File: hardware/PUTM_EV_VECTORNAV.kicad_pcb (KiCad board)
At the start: 2 copper layers, 60 x 40 mm, 4 parts

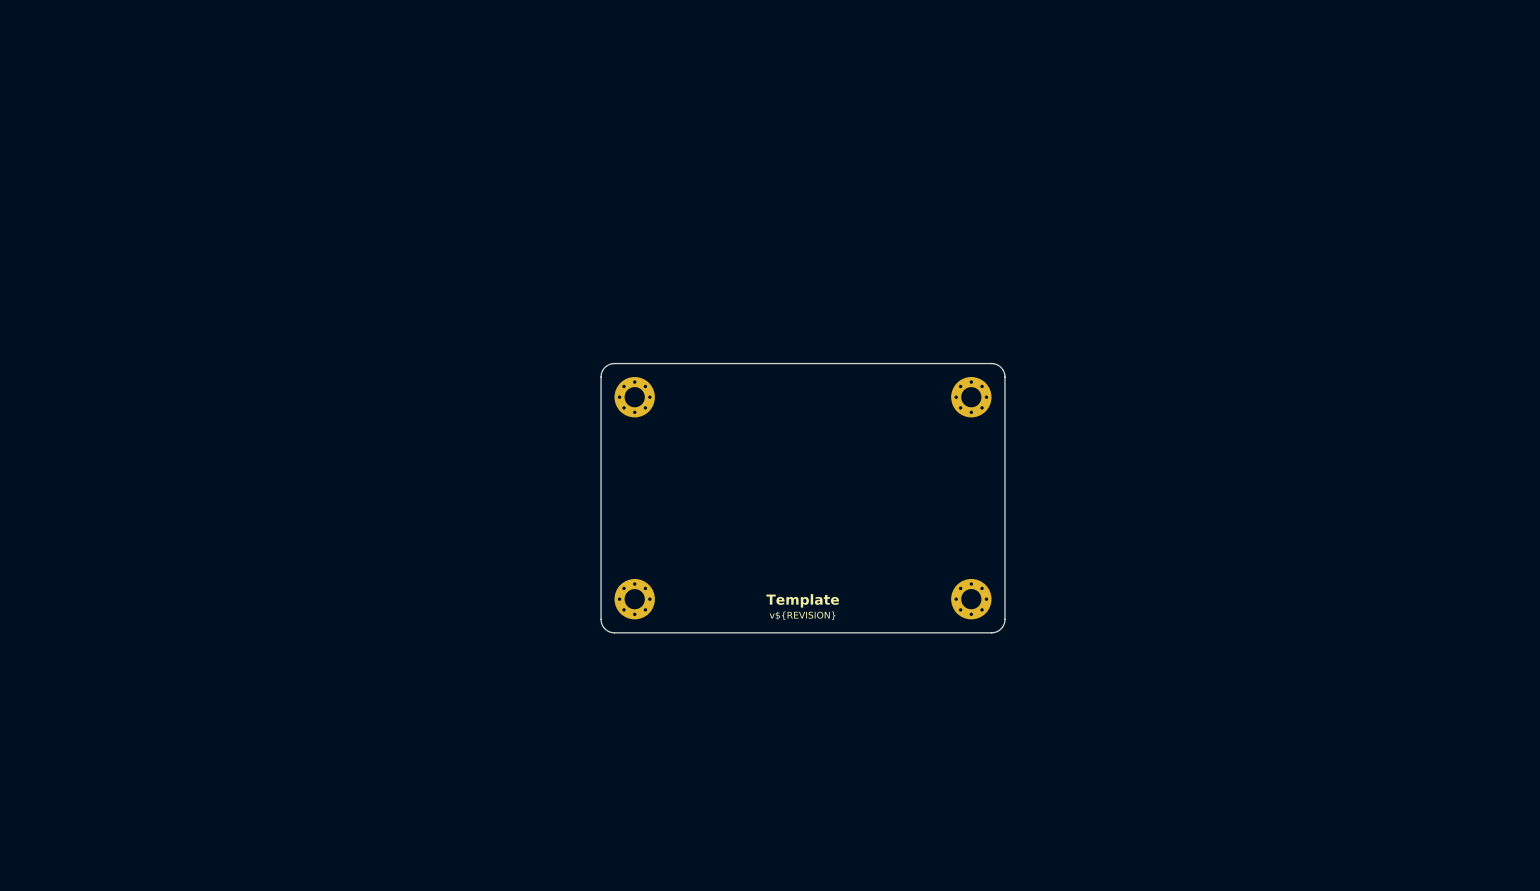
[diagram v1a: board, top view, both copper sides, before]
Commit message: 3D models, optocoupler added, pcb settings and components placing
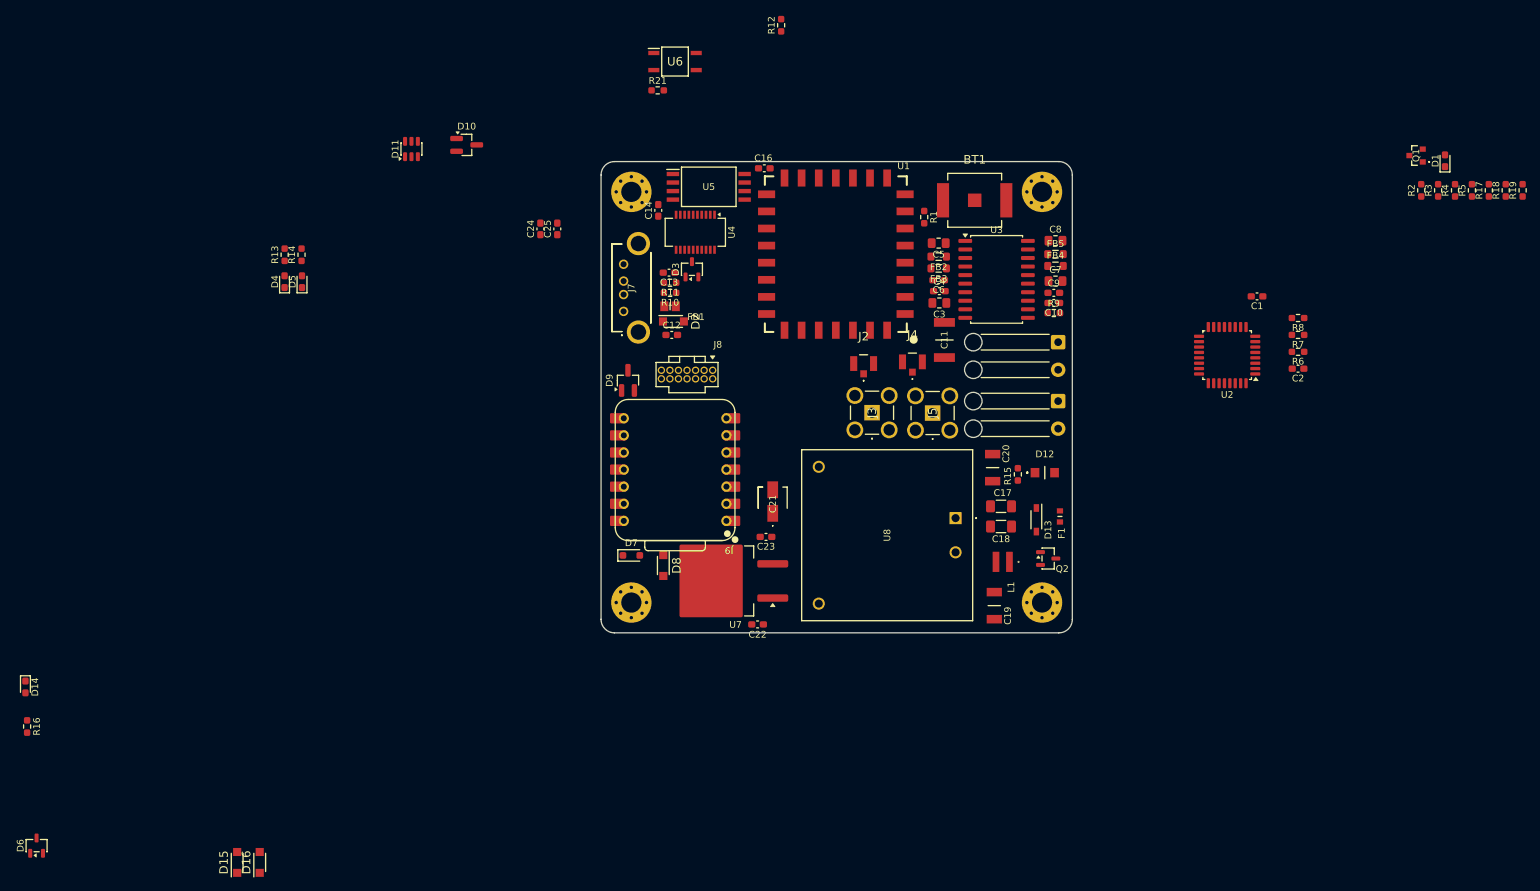
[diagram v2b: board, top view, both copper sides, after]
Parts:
- added BT1: Battery_Cell, BatteryHolder:2998TR, F.Cu at (171.5, 51.8)
- added C1: 100nF, Capacitor_SMD:C_0603_1608Metric_Pad1.08x0.95mm_HandSolder, F.Cu at (213.4, 66.0)
- added C10: 10nF, Capacitor_SMD:C_0603_1608Metric_Pad1.08x0.95mm_HandSolder, F.Cu at (183.2, 67.0)
- added C11: 4.7nF/Y2, samacsys:CAPC5728X280N, F.Cu at (167.0, 72.5)
- added C12: 10nF, Capacitor_SMD:C_0603_1608Metric_Pad1.08x0.95mm_HandSolder, F.Cu at (126.5, 71.8)
- added C13: 100nF, Capacitor_SMD:C_0603_1608Metric_Pad1.08x0.95mm_HandSolder, F.Cu at (126.1, 62.5)
- added C14: 10nF, Capacitor_SMD:C_0603_1608Metric_Pad1.08x0.95mm_HandSolder, F.Cu at (124.5, 53.2)
- added C16: 10nF, Capacitor_SMD:C_0603_1608Metric_Pad1.08x0.95mm_HandSolder, F.Cu at (140.2, 47.0)
- added C17: 2.2uF, Capacitor_SMD:C_1206_3216Metric_Pad1.33x1.80mm_HandSolder, F.Cu at (175.4, 97.2)
- added C18: 2.2uF, Capacitor_SMD:C_1206_3216Metric_Pad1.33x1.80mm_HandSolder, F.Cu at (175.4, 100.2)
- added C19: 150pF X2/Y3, 150pFCaps:CAPC4620X165N, F.Cu at (174.4, 112.0)
- added C2: 100nF, Capacitor_SMD:C_0603_1608Metric_Pad1.08x0.95mm_HandSolder, F.Cu at (219.5, 76.8)
- added C20: 150pF X2/Y3, 150pFCaps:CAPC4620X165N, F.Cu at (174.2, 91.5)
- added C21: 47uF+, 47uCapPolarized:EEE1AA220WR, F.Cu at (141.5, 96.5)
- added C22: 10uF, Capacitor_SMD:C_0603_1608Metric_Pad1.08x0.95mm_HandSolder, F.Cu at (139.2, 114.8)
- added C23: 10uF, Capacitor_SMD:C_0603_1608Metric_Pad1.08x0.95mm_HandSolder, F.Cu at (140.5, 101.8)
- added C24: 47pF, Capacitor_SMD:C_0603_1608Metric_Pad1.08x0.95mm_HandSolder, F.Cu at (107.0, 56.0)
- added C25: 47pF, Capacitor_SMD:C_0603_1608Metric_Pad1.08x0.95mm_HandSolder, F.Cu at (109.5, 56.0)
- added C3: 47uF, Capacitor_SMD:C_0805_2012Metric_Pad1.18x1.45mm_HandSolder, F.Cu at (166.2, 67.0)
- added C4: 100nF, Capacitor_SMD:C_0603_1608Metric_Pad1.08x0.95mm_HandSolder, F.Cu at (166.2, 65.2)
- added C5: 47uF, Capacitor_SMD:C_0805_2012Metric_Pad1.18x1.45mm_HandSolder, F.Cu at (166.2, 58.1)
- added C6: 10nF, Capacitor_SMD:C_0603_1608Metric_Pad1.08x0.95mm_HandSolder, F.Cu at (166.2, 63.6)
- added C7: 47uF, Capacitor_SMD:C_0805_2012Metric_Pad1.18x1.45mm_HandSolder, F.Cu at (183.5, 63.8)
- added C8: 47uF, Capacitor_SMD:C_0805_2012Metric_Pad1.18x1.45mm_HandSolder, F.Cu at (183.5, 57.8)
- added C9: 100nF, Capacitor_SMD:C_0603_1608Metric_Pad1.08x0.95mm_HandSolder, F.Cu at (183.2, 65.5)
- added D1: LED, Diode_SMD:D_0603_1608Metric_Pad1.05x0.95mm_HandSolder, F.Cu at (241.4, 45.9)
- added D10: 5V/360W, Package_TO_SOT_SMD:SOT-23_Handsoldering, F.Cu at (96.0, 43.5)
- added D11: 3.6V/85W, Package_TO_SOT_SMD:SOT-23-6, F.Cu at (87.8, 44.1)
- added D12: 26V, 24VinputTVS:SMFA2005CA, F.Cu at (181.9, 92.2)
- added D13: 10V, Zener10V:SOD3716X135N, F.Cu at (180.7, 99.2)
- added D14: LED, Diode_SMD:D_0603_1608Metric_Pad1.05x0.95mm_HandSolder, F.Cu at (30.5, 124.0)
- added D15: 5V/200W, 5Vtvs:SODFL3618X110N, F.Cu at (62.0, 150.1)
- added D16: 5V/200W, 5Vtvs:SODFL3618X110N, F.Cu at (65.3, 150.1)
- added D2: 5V/200W, 5Vtvs:SODFL3618X110N, F.Cu at (126.8, 69.8)
- added D3: 5V/140W, Package_TO_SOT_SMD:SOT-23-3, F.Cu at (129.5, 62.0)
- added D4: LED, Diode_SMD:D_0603_1608Metric_Pad1.05x0.95mm_HandSolder, F.Cu at (69.0, 63.8)
- added D5: LED, Diode_SMD:D_0603_1608Metric_Pad1.05x0.95mm_HandSolder, F.Cu at (71.6, 63.8)
- added D6: 27V/420W, Package_TO_SOT_SMD:SOT-23-3, F.Cu at (32.2, 147.6)
- added D7: NSVRB751V40T1G, Diode_SMD:D_SOD-323_HandSoldering, F.Cu at (120.5, 104.5)
- added D8: 5V/200W, 5Vtvs:SODFL3618X110N, F.Cu at (125.2, 106.0)
- added D9: 5V/360W, Package_TO_SOT_SMD:SOT-23_Handsoldering, F.Cu at (120.0, 78.5)
- added F1: 250mA, 24V250mAFuse:FUSC1608X43N, F.Cu at (184.2, 98.7)
- added FB1: 40R@100MHz, FerriteUSB:BEADC2012X110N, F.Cu at (126.2, 67.5)
- added FB2: 2K@100MHz, Inductor_SMD:L_0805_2012Metric_Pad1.05x1.20mm_HandSolder, F.Cu at (166.2, 60.1)
- added FB3: 2K@100MHz, Inductor_SMD:L_0805_2012Metric_Pad1.05x1.20mm_HandSolder, F.Cu at (166.2, 61.9)
- added FB4: 2K@100MHz, Inductor_SMD:L_0805_2012Metric_Pad1.05x1.20mm_HandSolder, F.Cu at (183.5, 61.5)
- added FB5: 2K@100MHz, Inductor_SMD:L_0805_2012Metric_Pad1.05x1.20mm_HandSolder, F.Cu at (183.5, 59.8)
- added J1: Conn_01x02, StrainRelief:StrainRelief, F.Cu at (183.9, 72.8)
- added J2: uFL ant, antenna:CONUFL001SMDT, F.Cu at (155.0, 76.0)
- added J3: SMA ant, antenna:SMACONNECTOR, F.Cu at (156.2, 83.3)
- added J4: uFL ant, antenna:CONUFL001SMDT, F.Cu at (162.2, 75.8)
- added J5: SMA ant, antenna:SMACONNECTOR, F.Cu at (165.2, 83.3)
- added J6: Conn_01x02, StrainRelief:StrainRelief, F.Cu at (183.9, 81.6)
- added J7: USB_A, USBAconnector:UJ2AV4TH, F.Cu at (119.3, 68.2)
- added J8: FTSH-107-01-L-D-K, samacsys:FTSH-107-XX-YYY-D-K, F.Cu at (128.8, 77.6)
- added J9: XIAO ESP32S3 Sense, samacsys:XIAO-ESP32S3-DIP, F.Cu at (127.0, 91.8)
- added L1: 10uH, inductor:VLS3010, F.Cu at (175.7, 105.5)
- added Q1: NMOS, VNlednmos:DMN63D8L13, F.Cu at (237.1, 45.1)
- added Q2: SI2347DS-T1-GE3, Package_TO_SOT_SMD:SOT-23-3, F.Cu at (182.4, 105.0)
- added R1: 1k, Resistor_SMD:R_0603_1608Metric_Pad0.98x0.95mm_HandSolder, F.Cu at (164.0, 54.2)
- added R10: 27R, Resistor_SMD:R_0603_1608Metric_Pad0.98x0.95mm_HandSolder, F.Cu at (126.2, 65.5)
- added R11: 27R, Resistor_SMD:R_0603_1608Metric_Pad0.98x0.95mm_HandSolder, F.Cu at (126.2, 64.0)
- added R12: 10k, Resistor_SMD:R_0603_1608Metric_Pad0.98x0.95mm_HandSolder, F.Cu at (142.8, 25.8)
- added R13: 330R, Resistor_SMD:R_0603_1608Metric_Pad0.98x0.95mm_HandSolder, F.Cu at (69.0, 59.8)
- added R14: 330R, Resistor_SMD:R_0603_1608Metric_Pad0.98x0.95mm_HandSolder, F.Cu at (71.5, 59.8)
- added R15: 100k, Resistor_SMD:R_0603_1608Metric_Pad0.98x0.95mm_HandSolder, F.Cu at (177.9, 92.5)
- added R16: 330R, Resistor_SMD:R_0603_1608Metric_Pad0.98x0.95mm_HandSolder, F.Cu at (30.8, 129.9)
- added R17: 100R, Resistor_SMD:R_0603_1608Metric_Pad0.98x0.95mm_HandSolder, F.Cu at (247.9, 50.3)
- added R18: 100R, Resistor_SMD:R_0603_1608Metric_Pad0.98x0.95mm_HandSolder, F.Cu at (250.4, 50.3)
- added R19: 100R, Resistor_SMD:R_0603_1608Metric_Pad0.98x0.95mm_HandSolder, F.Cu at (252.9, 50.3)
- added R2: 33R, Resistor_SMD:R_0603_1608Metric_Pad0.98x0.95mm_HandSolder, F.Cu at (237.8, 50.3)
- added R21: 1k, Resistor_SMD:R_0603_1608Metric_Pad0.98x0.95mm_HandSolder, F.Cu at (124.4, 35.4)
- added R3: 330R, Resistor_SMD:R_0603_1608Metric_Pad0.98x0.95mm_HandSolder, F.Cu at (240.3, 50.3)
- added R4: 100R, Resistor_SMD:R_0603_1608Metric_Pad0.98x0.95mm_HandSolder, F.Cu at (242.8, 50.3)
- added R5: 10k, Resistor_SMD:R_0603_1608Metric_Pad0.98x0.95mm_HandSolder, F.Cu at (245.4, 50.3)
- added R6: 33R, Resistor_SMD:R_0603_1608Metric_Pad0.98x0.95mm_HandSolder, F.Cu at (219.5, 74.3)
- added R7: 33R, Resistor_SMD:R_0603_1608Metric_Pad0.98x0.95mm_HandSolder, F.Cu at (219.5, 71.7)
- added R8: 33R, Resistor_SMD:R_0603_1608Metric_Pad0.98x0.95mm_HandSolder, F.Cu at (219.5, 69.2)
- added R9: 0R, Resistor_SMD:R_0603_1608Metric_Pad0.98x0.95mm_HandSolder, F.Cu at (183.2, 68.5)
- added U1: VN-300, VN300:7X8CASTLE, F.Cu at (151.0, 59.8)
- added U2: STM32G0C1KCTxN, Package_QFP:LQFP-32_7x7mm_P0.8mm, F.Cu at (209.0, 74.8)
- added U3: ADM3057ExRW, Package_SO:SOIC-20W_7.5x12.8mm_P1.27mm, F.Cu at (174.8, 63.5)
- added U4: FT231XS-U, Package_SO:SSOP-20_3.9x8.7mm_P0.635mm, F.Cu at (130.0, 56.5)
- added U5: API7721FSB-13, iso_conv:SOIC127P1150X280-8N, F.Cu at (132.0, 49.8)
- added U6: AQY284S, OptoCoupler:SOP254P680X230-4N, F.Cu at (127.0, 31.1)
- added U7: NCP565D2T33R4G, Package_TO_SOT_SMD:TO-263-2, F.Cu at (133.8, 108.3)
- added U8: SI06W8-05, DCisoconv:SI06W805, F.Cu at (168.7, 99.0)
- moved REF** 32.3 mm to (181.5, 50.5)
- moved REF** 30.5 mm to (120.5, 50.5)
- moved REF** 10.5 mm to (181.5, 111.5)
- moved REF** 0.71 mm to (120.5, 111.5)
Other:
- board size 60 x 40 mm -> 70 x 70 mm
- copper layers 2 -> 4
- board text removed: "Template"
- board text removed: "v${REVISION}"

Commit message: All components placed on pcb
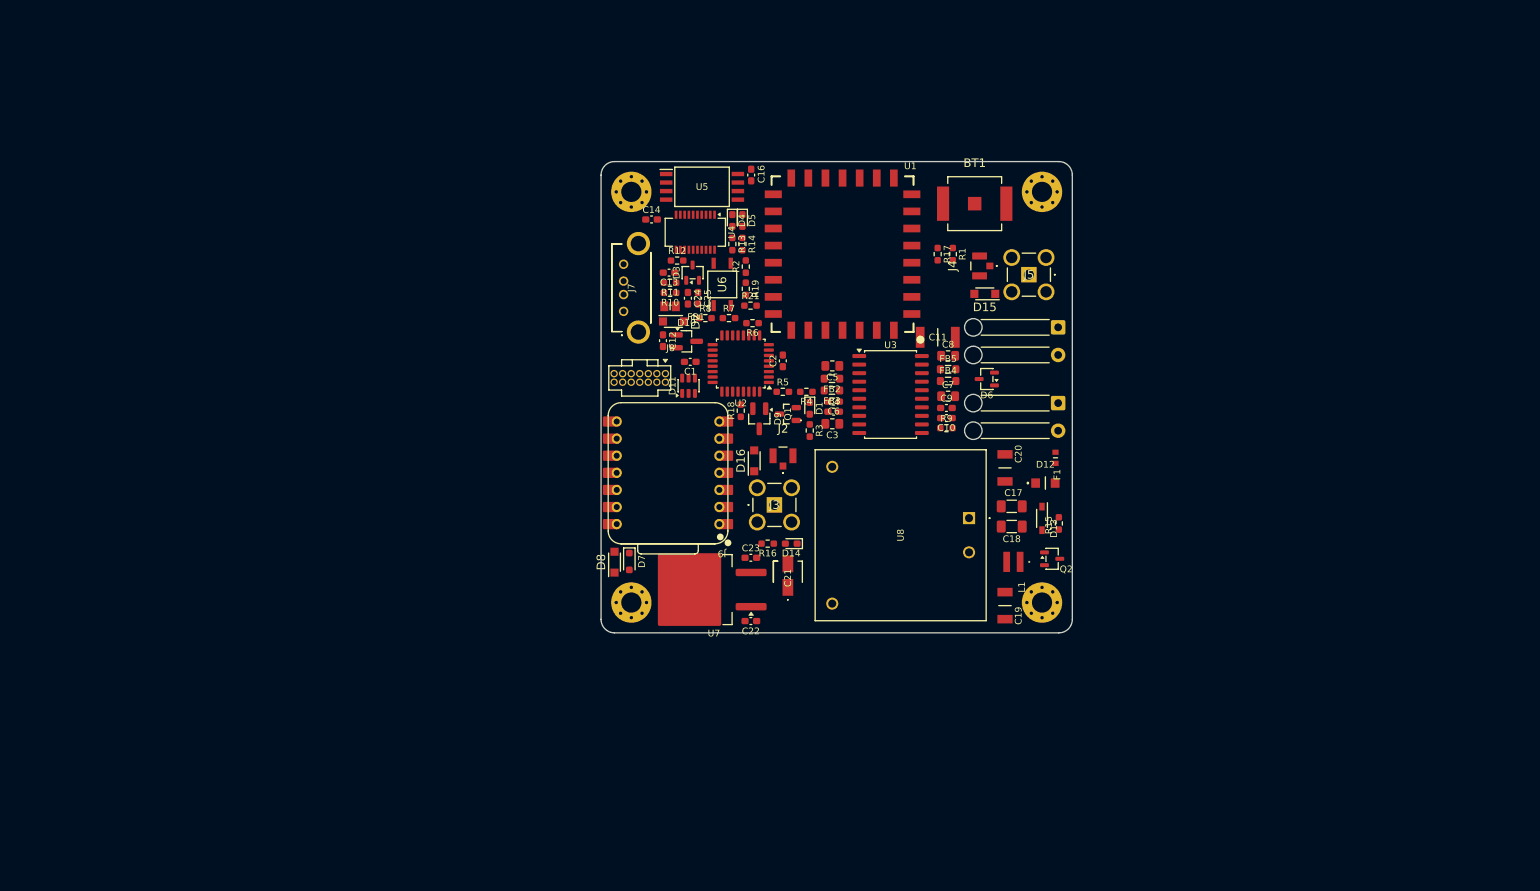
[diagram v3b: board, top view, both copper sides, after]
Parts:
- U7: footprint Package_TO_SOT_SMD:TO-263-2 -> 5VLDO3V3:TO-263-2
- moved D6 157.2 mm to (173.3, 78.3), turned to 180 degrees
- moved D15 139.5 mm to (173.0, 65.7), turned to 180 degrees
- moved R18 118.2 mm to (136.8, 83.0)
- moved R19 116.3 mm to (137.5, 64.9), turned to -90 degrees
- moved D14 115.7 mm to (144.2, 102.8), turned to 180 degrees
- moved R16 113.3 mm to (140.8, 102.8), turned to 180 degrees
- moved R5 106.6 mm to (143.0, 80.2), turned to 0 degrees
- moved D1 101.3 mm to (147.0, 82.7), turned to -90 degrees
- moved R2 101.0 mm to (137.5, 61.6)
- moved Q1 100.9 mm to (143.8, 83.5)
- moved R4 100.9 mm to (146.5, 80.2), turned to 180 degrees
- moved R3 99.9 mm to (147.0, 86.0), turned to -90 degrees
- moved D16 94.6 mm to (138.8, 90.5)
- moved R8 88.0 mm to (131.5, 69.2), turned to 0 degrees
- moved C1 84.7 mm to (129.2, 75.8)
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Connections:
- D11 pad 3: /Connectors/PROG_SWDIO -> /Connectors/PROG_SWCLK
- D11 pad 4: /Connectors/PROG_SWCLK -> /Connectors/PROG_SWDIO
- D9 pad 1: /Connectors/XIAO_RX -> /Connectors/XIAO_TX
- D9 pad 2: /Connectors/XIAO_TX -> /Connectors/XIAO_RX
- R12 pad 2: /Connectors/USB_RST -> /Connectors/usbRST
- R6 pad 2: /MCU/VN_CS -> /MCU/vnCS
- R7 pad 2: /MCU/VN_SCK -> /MCU/vnSCK
- R8 pad 2: /MCU/VN_MOSI -> /MCU/vnMOSI
- U2 pad 11: /MCU/VN_CS -> /MCU/vnCS
- U2 pad 12: /MCU/VN_SCK -> /MCU/vnSCK
- U2 pad 14: /MCU/VN_MOSI -> /MCU/vnMOSI
- U4 pad 14: /Connectors/USB_RST -> /Connectors/usbRST
- U6 pad 4: /Connectors/USB_RST -> /Connectors/usbRST

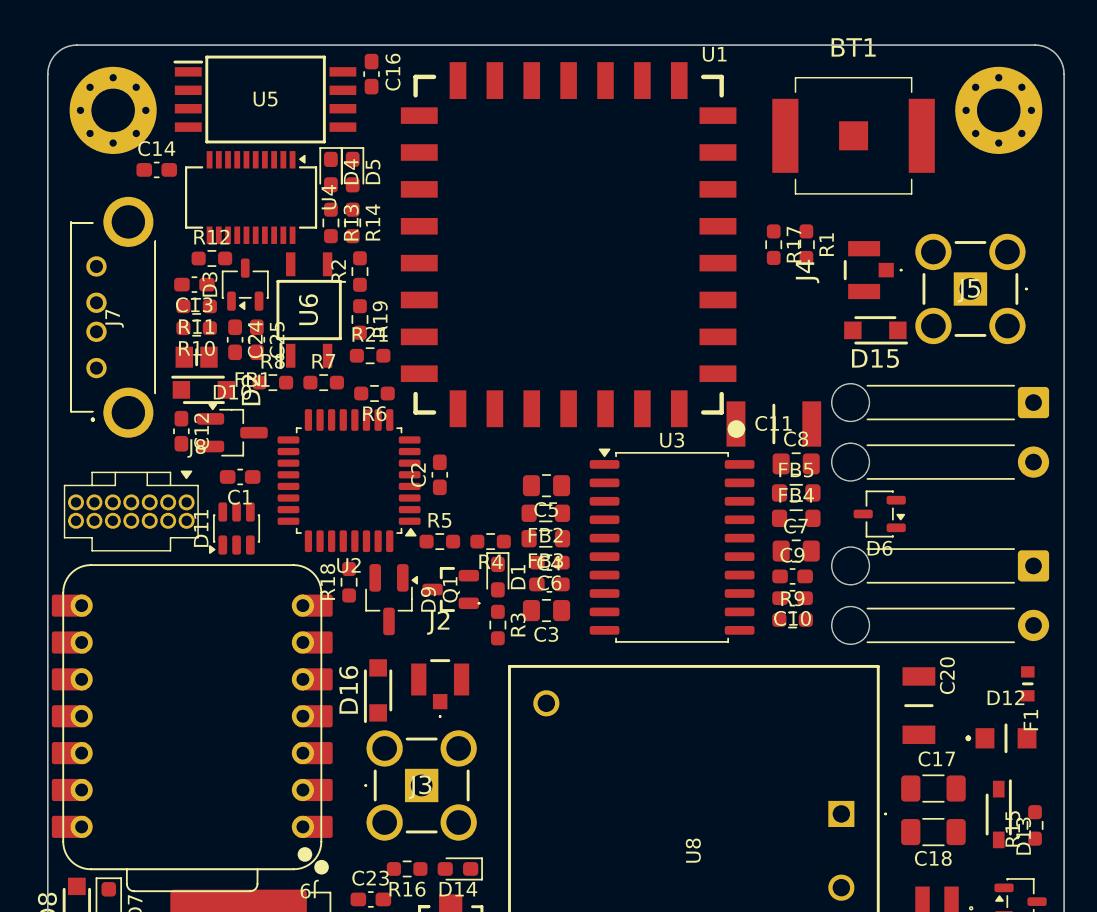
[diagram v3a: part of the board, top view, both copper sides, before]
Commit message: MCU and VN-300 routed
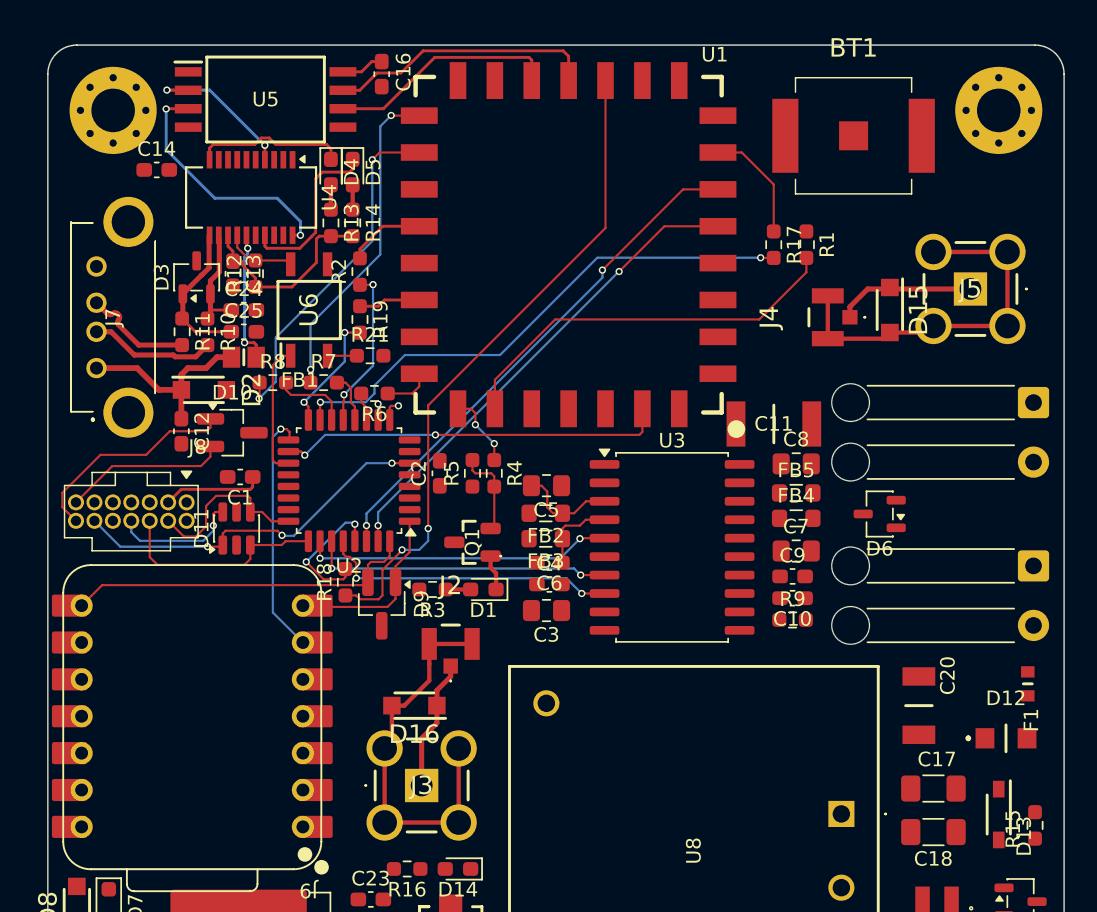
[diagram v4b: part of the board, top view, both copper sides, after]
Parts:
- moved R5 5.21 mm to (145.2, 75.5), turned to 90 degrees
- moved R3 5.12 mm to (142.5, 83.5), turned to 180 degrees
- moved R4 4.71 mm to (146.8, 75.5), turned to -90 degrees
- moved J4 4.10 mm to (169.7, 64.8)
- moved Q1 3.58 mm to (145.2, 80.2)
- moved D3 3.39 mm to (126.2, 62.0)
- moved FB1 3.25 mm to (129.5, 67.5)
- moved R12 3.18 mm to (130.3, 61.8), turned to 90 degrees
- moved C13 2.75 mm to (128.8, 61.8), turned to -90 degrees
- moved D16 2.71 mm to (141.2, 91.5), turned to 180 degrees
- moved J2 2.56 mm to (143.8, 87.2)
- moved C24 2.14 mm to (129.5, 64.2), turned to 0 degrees
- moved R11 2.02 mm to (125.2, 65.8), turned to -90 degrees
- moved D15 1.72 mm to (174.0, 64.2), turned to -90 degrees
- moved D1 1.31 mm to (146.0, 83.5), turned to 180 degrees
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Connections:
- net Net-(D15-A1) renamed /Connectors/RF2
- net Net-(D16-A1) renamed /Connectors/RF1
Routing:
- net Net-(U1-ENABLE): track 0.00 -> 45.3 mm, vias 0 -> 2
- net /MCU/VN_RESTORE: track 0.00 -> 36.9 mm, vias 0 -> 2
- net /MCU/VN_TX: track 0.00 -> 35.7 mm, vias 0 -> 2
- net /MCU/VN_RX: track 0.00 -> 33.6 mm, vias 0 -> 2
- net Net-(U1-VBAT): track 0.00 -> 27.5 mm
- net Net-(D16-A2): track 0.00 -> 27.2 mm
- net /MCU/VN_GNSS_SYNC: track 0.00 -> 26.7 mm, vias 0 -> 2
- net Net-(D15-A2): track 0.00 -> 25.9 mm
- net /Connectors/PROG_NRST: track 0.00 -> 25.6 mm, vias 0 -> 3
- net /Connectors/XIAO_RX: track 0.00 -> 24.4 mm
- net /MCU/VN_MOSI: track 0.00 -> 24.2 mm, vias 0 -> 2
- net /MCU/VN_SCK: track 0.00 -> 22.6 mm, vias 0 -> 2
- net /CAN/CAN_RX: track 0.00 -> 21.3 mm, vias 0 -> 2
- net /CAN/CAN_TX: track 0.00 -> 20.9 mm, vias 0 -> 2
- net /CAN/CAN_STBY: track 0.00 -> 20.6 mm, vias 0 -> 2
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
